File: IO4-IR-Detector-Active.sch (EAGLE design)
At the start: 32 parts, among them Q1 NPN-2222, Q2 NPN-2222, Q3 NPN-2222, Q4 NPN-2222

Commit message: panelized
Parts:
- C3: device SPCoast:CAP-POLPTH-2MM -> SPCoast:CAP-POL0810

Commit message: added values for connectors
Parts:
- CON1: value (none) -> RJ12/6
- JP1, JP2, JP3, JP4: value (none) -> 0.100
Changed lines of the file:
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@@
 <grid distance="100" unitdist="mil" unit="mil" style="dots" multiple="1" display="yes" altdistance="50" altunitdist="mil" altunit="mil"/>
 <layers>
-<layer number="1" name="Top" color="4" fill="1" visible="yes" active="no"/>
-<layer number="2" name="Route2" color="1" fill="3" visible="yes" active="no"/>
-<layer number="3" name="Route3" color="4" fill="3" visible="yes" active="no"/>
-<layer number="4" name="Route4" color="1" fill="4" visible="yes" active="no"/>
-<layer number="5" name="Route5" color="4" fill="4" visible="yes" active="no"/>
-<layer number="6" name="Route6" color="1" fill="8" visible="yes" active="no"/>
-<layer number="7" name="Route7" color="4" fill="8" visible="yes" active="no"/>
-<layer number="8" name="Route8" color="1" fill="2" visible="yes" active="no"/>
-<layer number="9" name="Route9" color="4" fill="2" visible="yes" active="no"/>
-<layer number="10" name="Route10" color="1" fill="7" visible="yes" active="no"/>
-<layer number="11" name="Route11" color="4" fill="7" visible="yes" active="no"/>
-<layer number="12" name="Route12" color="1" fill="5" visible="yes" active="no"/>
-<layer number="13" name="Route13" color="4" fill="5" visible="yes" active="no"/>
-<layer number="14" name="Route14" color="1" fill="6" visible="yes" active="no"/>
-<layer number="15" name="Route15" color="4" fill="6" visible="yes" active="no"/>
-<layer number="16" name="Bottom" color="2" fill="1" visible="yes" active="no"/>
-<layer number="17" name="Pads" color="23" fill="1" visible="yes" active="no"/>
-<layer number="18" name="Vias" color="29" fill="1" visible="yes" active="no"/>
-<layer number="19" name="Unrouted" color="6" fill="1" visible="yes" active="no"/>
-<layer number="20" name="Dimension" color="15" fill="1" visible="yes" active="no"/>
-<layer number="21" name="tPlace" color="19" fill="1" visible="yes" active="no"/>
-<layer number="22" name="bPlace" color="17" fill="1" visible="yes" active="no"/>
-<layer number="23" name="tOrigins" color="30" fill="1" visible="yes" active="no"/>
-<layer number="24" name="bOrigins" color="15" fill="1" visible="yes" active="no"/>
-<layer number="25" name="tNames" color="63" fill="1" visible="yes" active="no"/>
-<layer number="26" name="bNames" color="34" fill="1" visible="yes" active="no"/>
-<layer number="27" name="tValues" color="56" fill="1" visible="yes" active="no"/>
-<layer number="28" name="bValues" color="7" fill="1" visible="yes" active="no"/>
+<layer number="1" name="Top" color="4" fill="1" visible="no" active="no"/>
+<layer number="2" name="Route2" color="1" fill="3" visible="no" active="no"/>
+<layer number="3" name="Route3" color="4" fill="3" visible="no" active="no"/>
+<layer number="4" name="Route4" color="1" fill="4" visible="no" active="no"/>
+<layer number="5" name="Route5" color="4" fill="4" visible="no" active="no"/>
+<layer number="6" name="Route6" color="1" fill="8" visible="no" active="no"/>
+<layer number="7" name="Route7" color="4" fill="8" visible="no" active="no"/>
+<layer number="8" name="Route8" color="1" fill="2" visible="no" active="no"/>
+<layer number="9" name="Route9" color="4" fill="2" visible="no" active="no"/>
+<layer number="10" name="Route10" color="1" fill="7" visible="no" active="no"/>
+<layer number="11" name="Route11" color="4" fill="7" visible="no" active="no"/>
+<layer number="12" name="Route12" color="1" fill="5" visible="no" active="no"/>
+<layer number="13" name="Route13" color="4" fill="5" visible="no" active="no"/>
+<layer number="14" name="Route14" color="1" fill="6" visible="no" active="no"/>
+<layer number="15" name="Route15" color="4" fill="6" visible="no" active="no"/>
+<layer number="16" name="Bottom" color="2" fill="1" visible="no" active="no"/>
+<layer number="17" name="Pads" color="23" fill="1" visible="no" active="no"/>
+<layer number="18" name="Vias" color="29" fill="1" visible="no" active="no"/>
+<layer number="19" name="Unrouted" color="6" fill="1" visible="no" active="no"/>
+<layer number="20" name="Dimension" color="15" fill="1" visible="no" active="no"/>
+<layer number="21" name="tPlace" color="19" fill="1" visible="no" active="no"/>
+<layer number="22" name="bPlace" color="17" fill="1" visible="no" active="no"/>
+<layer number="23" name="tOrigins" color="30" fill="1" visible="no" active="no"/>
+<layer number="24" name="bOrigins" color="15" fill="1" visible="no" active="no"/>
+<layer number="25" name="tNames" color="63" fill="1" visible="no" active="no"/>
+<layer number="26" name="bNames" color="34" fill="1" visible="no" active="no"/>
+<layer number="27" name="tValues" color="56" fill="1" visible="no" active="no"/>
+<layer number="28" name="bValues" color="7" fill="1" visible="no" active="no"/>
 <layer number="29" name="tStop" color="7" fill="3" visible="no" active="no"/>
 <layer number="30" name="bStop" color="7" fill="6" visible="no" active="no"/>
@@
 <layer number="35" name="tGlue" color="7" fill="4" visible="no" active="no"/>
 <layer number="36" name="bGlue" color="7" fill="5" visible="no" active="no"/>
-<layer number="37" name="tTest" color="7" fill="1" visible="yes" active="no"/>
-<layer number="38" name="bTest" color="7" fill="1" visible="yes" active="no"/>
+<layer number="37" name="tTest" color="7" fill="1" visible="no" active="no"/>
+<layer number="38" name="bTest" color="7" fill="1" visible="no" active="no"/>
 <layer number="39" name="tKeepout" color="4" fill="11" visible="no" active="no"/>
 <layer number="40" name="bKeepout" color="3" fill="11" visible="no" active="no"/>
@@
 <layer number="44" name="Drills" color="16" fill="1" visible="no" active="no"/>
 <layer number="45" name="Holes" color="35" fill="1" visible="no" active="no"/>
-<layer number="46" name="Milling" color="35" fill="1" visible="yes" active="no"/>
-<layer number="47" name="Measures" color="21" fill="1" visible="yes" active="no"/>
-<layer number="48" name="Document" color="36" fill="1" visible="yes" active="no"/>
-<layer number="49" name="Reference" color="48" fill="1" visible="yes" active="no"/>
-<layer number="50" name="dxf" color="7" fill="1" visible="yes" active="no"/>
-<layer number="51" name="tDocu" color="24" fill="1" visible="yes" active="no"/>
-<layer number="52" name="bDocu" color="7" fill="1" visible="yes" active="no"/>
-<layer number="53" name="tGND_GNDA" color="7" fill="9" visible="yes" active="no"/>
-<layer number="54" name="bGND_GNDA" color="1" fill="9" visible="yes" active="no"/>
-<layer number="56" name="wert" color="7" fill="1" visible="yes" active="no"/>
-<layer number="57" name="tCAD" color="7" fill="1" visible="yes" active="no"/>
-<layer number="59" name="tCarbon" color="7" fill="1" visible="yes" active="no"/>
-<layer number="60" name="bCarbon" color="7" fill="1" visible="yes" active="no"/>
+<layer number="46" name="Milling" color="35" fill="1" visible="no" active="no"/>
+<layer number="47" name="Measures" color="21" fill="1" visible="no" active="no"/>
+<layer number="48" name="Document" color="36" fill="1" visible="no" active="no"/>
+<layer number="49" name="Reference" color="48" fill="1" visible="no" active="no"/>
+<layer number="50" name="dxf" color="7" fill="1" visible="no" active="no"/>
+<layer number="51" name="tDocu" color="24" fill="1" visible="no" active="no"/>
+<layer number="52" name="bDocu" color="7" fill="1" visible="no" active="no"/>
+<layer number="53" name="tGND_GNDA" color="7" fill="9" visible="no" active="no"/>
+<layer number="54" name="bGND_GNDA" color="1" fill="9" visible="no" active="no"/>
+<layer number="56" name="wert" color="7" fill="1" visible="no" active="no"/>
+<layer number="57" name="tCAD" color="7" fill="1" visible="no" active="no"/>
+<layer number="59" name="tCarbon" color="7" fill="1" visible="no" active="no"/>
+<layer number="60" name="bCarbon" color="7" fill="1" visible="no" active="no"/>
 <layer number="90" name="Modules" color="5" fill="1" visible="yes" active="yes"/>
 <layer number="91" name="Nets" color="2" fill="1" visible="yes" active="yes"/>
@@
 <part name="P+6" library="supply1" deviceset="V+" device=""/>
 <part name="P+7" library="supply1" deviceset="V+" device=""/>
-<part name="JP1" library="SPCoast" deviceset="CONNECTOR-M04" device="LOCK"/>
-<part name="JP2" library="SPCoast" deviceset="CONNECTOR-M04" device="LOCK"/>
+<part name="JP1" library="SPCoast" deviceset="CONNECTOR-M04" device="LOCK" value="0.100"/>
+<part name="JP2" library="SPCoast" deviceset="CONNECTOR-M04" device="LOCK" value="0.100"/>
 <part name="GND5" library="supply1" deviceset="GND" device=""/>
 <part name="R6" library="SPCoast" deviceset="R*" device="0805-RES" value="100K"/>
@@
 <part name="P+10" library="supply1" deviceset="V+" device=""/>
 <part name="P+11" library="supply1" deviceset="V+" device=""/>
-<part name="JP3" library="SPCoast" deviceset="CONNECTOR-M04" device="LOCK"/>
-<part name="JP4" library="SPCoast" deviceset="CONNECTOR-M04" device="LOCK"/>
+<part name="JP3" library="SPCoast" deviceset="CONNECTOR-M04" device="LOCK" value="0.100"/>
+<part name="JP4" library="SPCoast" deviceset="CONNECTOR-M04" device="LOCK" value="0.100"/>
 <part name="GND11" library="supply1" deviceset="GND" device=""/>
 <part name="R8" library="SPCoast" deviceset="R*" device="0805-RES" value="100K"/>
@@
 <part name="C1" library="SPCoast" deviceset="CAP*" device="0805" value="0.1uF"/>
 <part name="C2" library="SPCoast" deviceset="CAP*" device="0805" value="0.1uF"/>
-<part name="CON1" library="SPCoast" deviceset="CONNECTOR-RJ25" device="-6P6C"/>
+<part name="CON1" library="SPCoast" deviceset="CONNECTOR-RJ25" device="-6P6C" value="RJ12/6"/>
 </parts>
 <sheets>

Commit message: normalized values
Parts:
- ARDUINO1: value ARDUINO-PRO-MINIDAVESROBOT -> DAVEK
- C1, C2: device SPCoast:CAP0805 -> SPCoast:CAP0603
- R1, R10, R11, R12, R14, R2, R3, R4, R5, R6, R7, R8, R9: device SPCoast:R0805-RES -> SPCoast:R0603-RES
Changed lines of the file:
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@@
 <part name="OSH_LOGO" library="SparkFun" deviceset="OSHW-LOGO" device="M"/>
 <part name="GND6" library="supply1" deviceset="GND" device=""/>
-<part name="R1" library="SPCoast" deviceset="R*" device="0805-RES" value="1k0"/>
-<part name="R2" library="SPCoast" deviceset="R*" device="0805-RES" value="1k0"/>
+<part name="R1" library="SPCoast" deviceset="R*" device="0603-RES" value="1k0"/>
+<part name="R2" library="SPCoast" deviceset="R*" device="0603-RES" value="1k0"/>
 <part name="Q1" library="SPCoast" deviceset="NPN" device="-SOT23" value="NPN-2222"/>
 <part name="GND1" library="supply1" deviceset="GND" device=""/>
 <part name="GND2" library="supply1" deviceset="GND" device=""/>
-<part name="R5" library="SPCoast" deviceset="R*" device="0805-RES" value="100K"/>
+<part name="R5" library="SPCoast" deviceset="R*" device="0603-RES" value="100K"/>
 <part name="P+4" library="supply1" deviceset="V+" device=""/>
 <part name="P+5" library="supply1" deviceset="V+" device=""/>
@@
 <part name="JP2" library="SPCoast" deviceset="CONNECTOR-M04" device="LOCK" value="0.100"/>
 <part name="GND5" library="supply1" deviceset="GND" device=""/>
-<part name="R6" library="SPCoast" deviceset="R*" device="0805-RES" value="100K"/>
-<part name="R3" library="SPCoast" deviceset="R*" device="0805-RES" value="1k0"/>
-<part name="R4" library="SPCoast" deviceset="R*" device="0805-RES" value="1k0"/>
+<part name="R6" library="SPCoast" deviceset="R*" device="0603-RES" value="100K"/>
+<part name="R3" library="SPCoast" deviceset="R*" device="0603-RES" value="1k0"/>
+<part name="R4" library="SPCoast" deviceset="R*" device="0603-RES" value="1k0"/>
 <part name="Q3" library="SPCoast" deviceset="NPN" device="-SOT23" value="NPN-2222"/>
 <part name="GND7" library="supply1" deviceset="GND" device=""/>
 <part name="GND8" library="supply1" deviceset="GND" device=""/>
-<part name="R7" library="SPCoast" deviceset="R*" device="0805-RES" value="100K"/>
+<part name="R7" library="SPCoast" deviceset="R*" device="0603-RES" value="100K"/>
 <part name="P+8" library="supply1" deviceset="V+" device=""/>
 <part name="P+9" library="supply1" deviceset="V+" device=""/>
@@
 <part name="JP4" library="SPCoast" deviceset="CONNECTOR-M04" device="LOCK" value="0.100"/>
 <part name="GND11" library="supply1" deviceset="GND" device=""/>
-<part name="R8" library="SPCoast" deviceset="R*" device="0805-RES" value="100K"/>
+<part name="R8" library="SPCoast" deviceset="R*" device="0603-RES" value="100K"/>
 <part name="LED1" library="SPCoast" deviceset="LED*" device="0603-LED" value="Y"/>
 <part name="LED2" library="SPCoast" deviceset="LED*" device="0603-LED" value="Y"/>
 <part name="LED3" library="SPCoast" deviceset="LED*" device="0603-LED" value="Y"/>
 <part name="LED4" library="SPCoast" deviceset="LED*" device="0603-LED" value="Y"/>
-<part name="R9" library="SPCoast" deviceset="R*" device="0805-RES" value="2k0"/>
-<part name="R10" library="SPCoast" deviceset="R*" device="0805-RES" value="2k0"/>
-<part name="R11" library="SPCoast" deviceset="R*" device="0805-RES" value="2k0"/>
-<part name="R12" library="SPCoast" deviceset="R*" device="0805-RES" value="2k0"/>
+<part name="R9" library="SPCoast" deviceset="R*" device="0603-RES" value="2k0"/>
+<part name="R10" library="SPCoast" deviceset="R*" device="0603-RES" value="2k0"/>
+<part name="R11" library="SPCoast" deviceset="R*" device="0603-RES" value="2k0"/>
+<part name="R12" library="SPCoast" deviceset="R*" device="0603-RES" value="2k0"/>
 <part name="P+16" library="supply1" deviceset="V+" device=""/>
 <part name="Q4" library="SPCoast" deviceset="NPN" device="-SOT23" value="NPN-2222"/>
@@
 <part name="P+3" library="supply1" deviceset="V+" device=""/>
 <part name="LED5" library="SPCoast" deviceset="LED*" device="0603-LED" value="G"/>
-<part name="R14" library="SPCoast" deviceset="R*" device="0805-RES" value="2k0"/>
+<part name="R14" library="SPCoast" deviceset="R*" device="0603-RES" value="2k0"/>
 <part name="C3" library="SPCoast" deviceset="CAP-POL*" device="0810" value="220uF"/>
-<part name="ARDUINO1" library="SPCoast" deviceset="ARDUINO-PRO-MINI" device="DAVESROBOT"/>
+<part name="ARDUINO1" library="SPCoast" deviceset="ARDUINO-PRO-MINI" device="DAVESROBOT" value="DAVEK"/>
 <part name="P+1" library="supply1" deviceset="V+" device=""/>
 <part name="GND3" library="supply1" deviceset="GND" device=""/>
-<part name="C1" library="SPCoast" deviceset="CAP*" device="0805" value="0.1uF"/>
-<part name="C2" library="SPCoast" deviceset="CAP*" device="0805" value="0.1uF"/>
+<part name="C1" library="SPCoast" deviceset="CAP*" device="0603" value="0.1uF"/>
+<part name="C2" library="SPCoast" deviceset="CAP*" device="0603" value="0.1uF"/>
 <part name="CON1" library="SPCoast" deviceset="CONNECTOR-RJ25" device="-6P6C" value="RJ12/6"/>
 </parts>

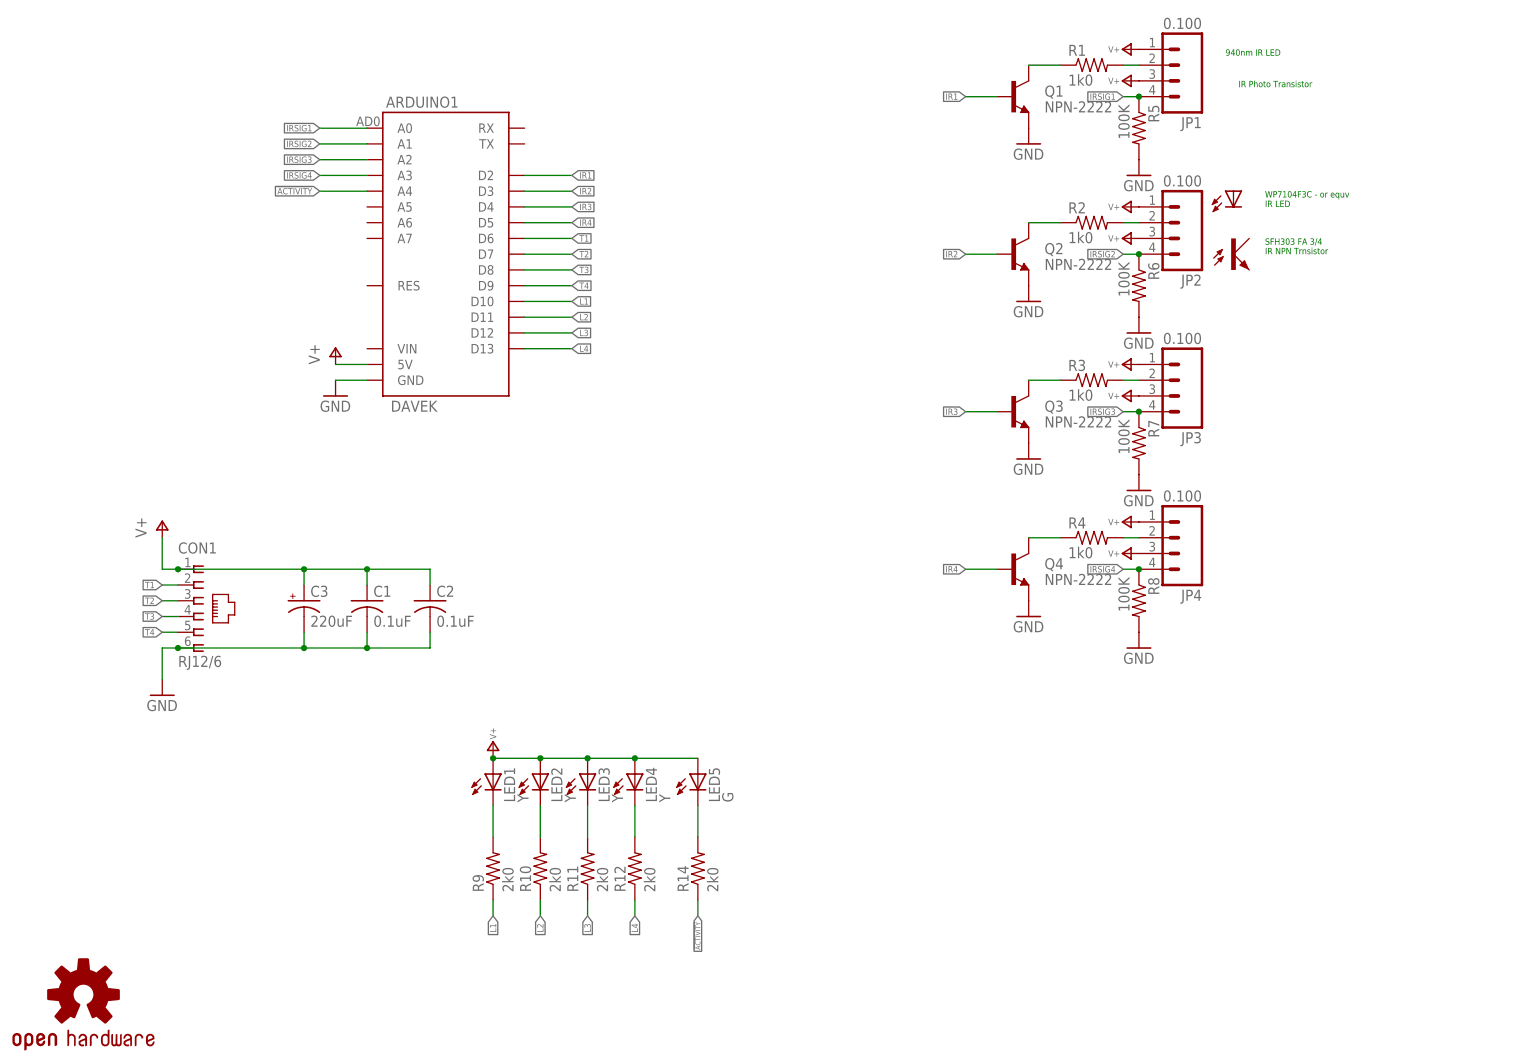
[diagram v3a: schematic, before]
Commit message: make room for conveyer fingers
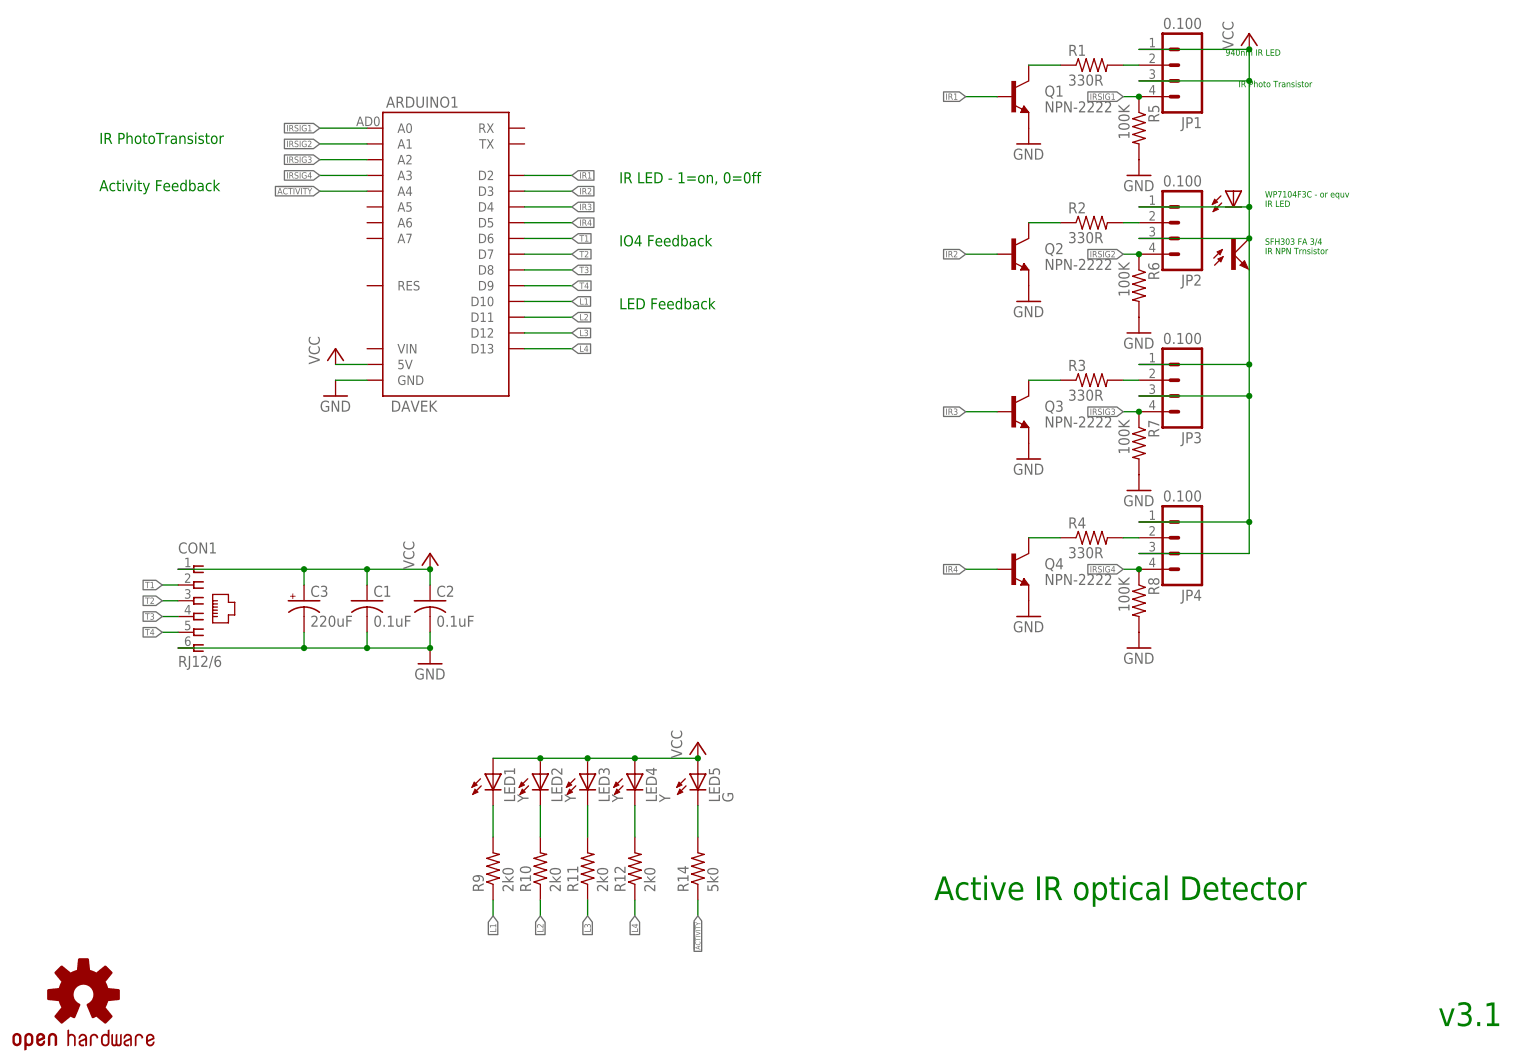
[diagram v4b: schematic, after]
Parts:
- OSH_LOGO: value OSHW-LOGOM -> DOC-OSHW-LOGO-S; device SparkFun:OSHW-LOGOM -> SPCoast:DOC-OSHW-LOGO-S
- R1, R2, R3, R4: value 1k0 -> 330R
- R14: value 2k0 -> 5k0
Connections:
- net V+ renamed VCC
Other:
- note added: "Active IR optical Detector"
- note added: "Activity Feedback"
- note added: "IO4 Feedback"
- note added: "IR LED - 1=on, 0=0ff"
- note added: "IR PhotoTransistor"
- note added: "LED Feedback"
- note added: "v3.1"
- note removed: "IOShield"
- note removed: "IR optical Detector"
- note removed: "v3.0"
